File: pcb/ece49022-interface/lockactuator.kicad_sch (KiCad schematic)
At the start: 0 parts

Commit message: lock shit
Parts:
- added D5: D, symbol Device:D
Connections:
- new net +12V: D5.1 (K)
- new net LOAD_RTN: D5.2 (A)

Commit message: save
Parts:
- D5: footprint (none) -> 49022_Footprints:SMFDO-219AB_VIS-L
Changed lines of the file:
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@@
 			)
 		)
-		(property "Footprint" ""
+		(property "Footprint" "49022_Footprints:SMFDO-219AB_VIS-L"
 			(at 74.93 55.88 0)
 			(effects
@@
 			)
 		)
-		(property "Description" "Diode"
+		(property "Description" "VS-E7FX0212HM3"
 			(at 74.93 55.88 0)
 			(effects

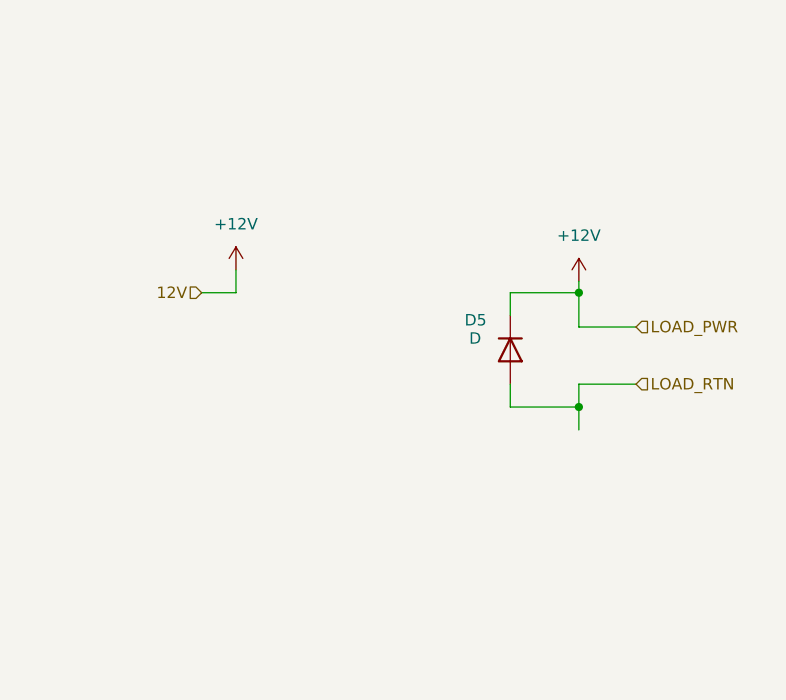
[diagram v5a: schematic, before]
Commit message: edited shelf power and added power for interface PCB
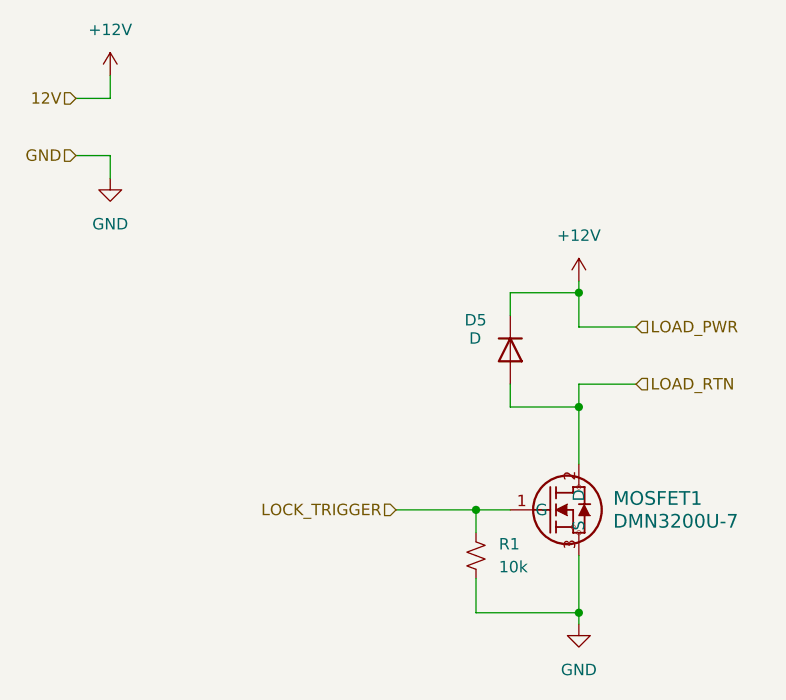
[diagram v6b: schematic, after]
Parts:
- added MOSFET1: DMN3200U-7, SOT23_DMN3200U_2P9X1P3_DIO, symbol ECE49022_Symbols:DMN3200U-7
- added R1: 10k, symbol Device:R_Small_US
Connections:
- net LOAD_RTN: now also MOSFET1.2 (D)
- new net GND: MOSFET1.3 (S), R1.2
- new net LOCK_TRIGGER: MOSFET1.1 (G), R1.1

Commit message: footprint update
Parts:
- R1: footprint (none) -> Resistor_SMD:R_0402_1005Metric
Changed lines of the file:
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@@
 			)
 		)
-		(property "Footprint" ""
+		(property "Footprint" "Resistor_SMD:R_0402_1005Metric"
 			(at 71.12 78.74 0)
 			(effects

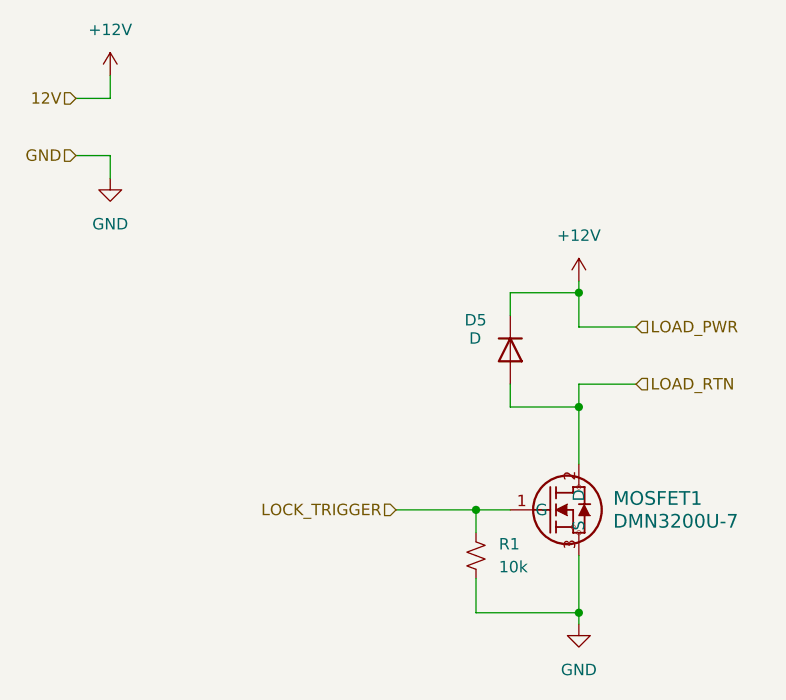
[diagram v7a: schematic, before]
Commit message: update resistor
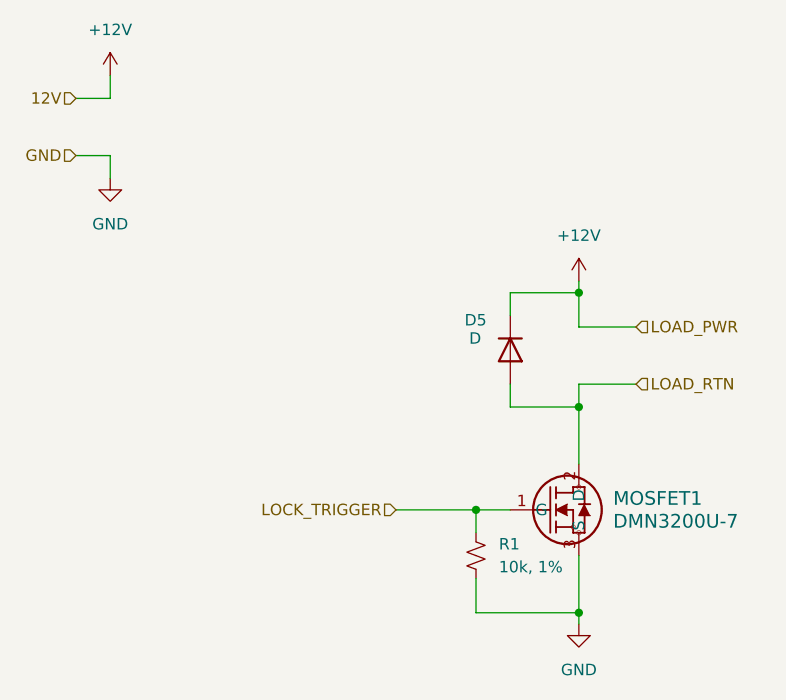
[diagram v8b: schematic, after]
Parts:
- R1: value 10k -> 10k, 1%; footprint Resistor_SMD:R_0402_1005Metric -> Resistor_SMD:R_0402_1005Metric_Pad0.72x0.64mm_HandSolder
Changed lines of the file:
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@@
 			)
 		)
-		(property "Value" "10k"
+		(property "Value" "10k, 1%"
 			(at 73.66 80.0099 0)
 			(effects
@@
 			)
 		)
-		(property "Footprint" "Resistor_SMD:R_0402_1005Metric"
+		(property "Footprint" "Resistor_SMD:R_0402_1005Metric_Pad0.72x0.64mm_HandSolder"
 			(at 71.12 78.74 0)
 			(effects
@@
 			)
 		)
-		(property "Description" "Resistor, small US symbol"
+		(property "Description" "RC0402FR-0710KL"
 			(at 71.12 78.74 0)
 			(effects
